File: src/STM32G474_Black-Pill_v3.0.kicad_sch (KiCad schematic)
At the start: 45 parts, among them J101 USB_C_Receptacle_USB2.0, J102 Conn_01x20, J103 Conn_01x20, J104 Conn_01x04, SW101 SW_Push, SW102 SW_Push, SW103 SW_Push, U101 W25Q32JVSS, U102 STM32G474RETx, U103 AP7343xx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

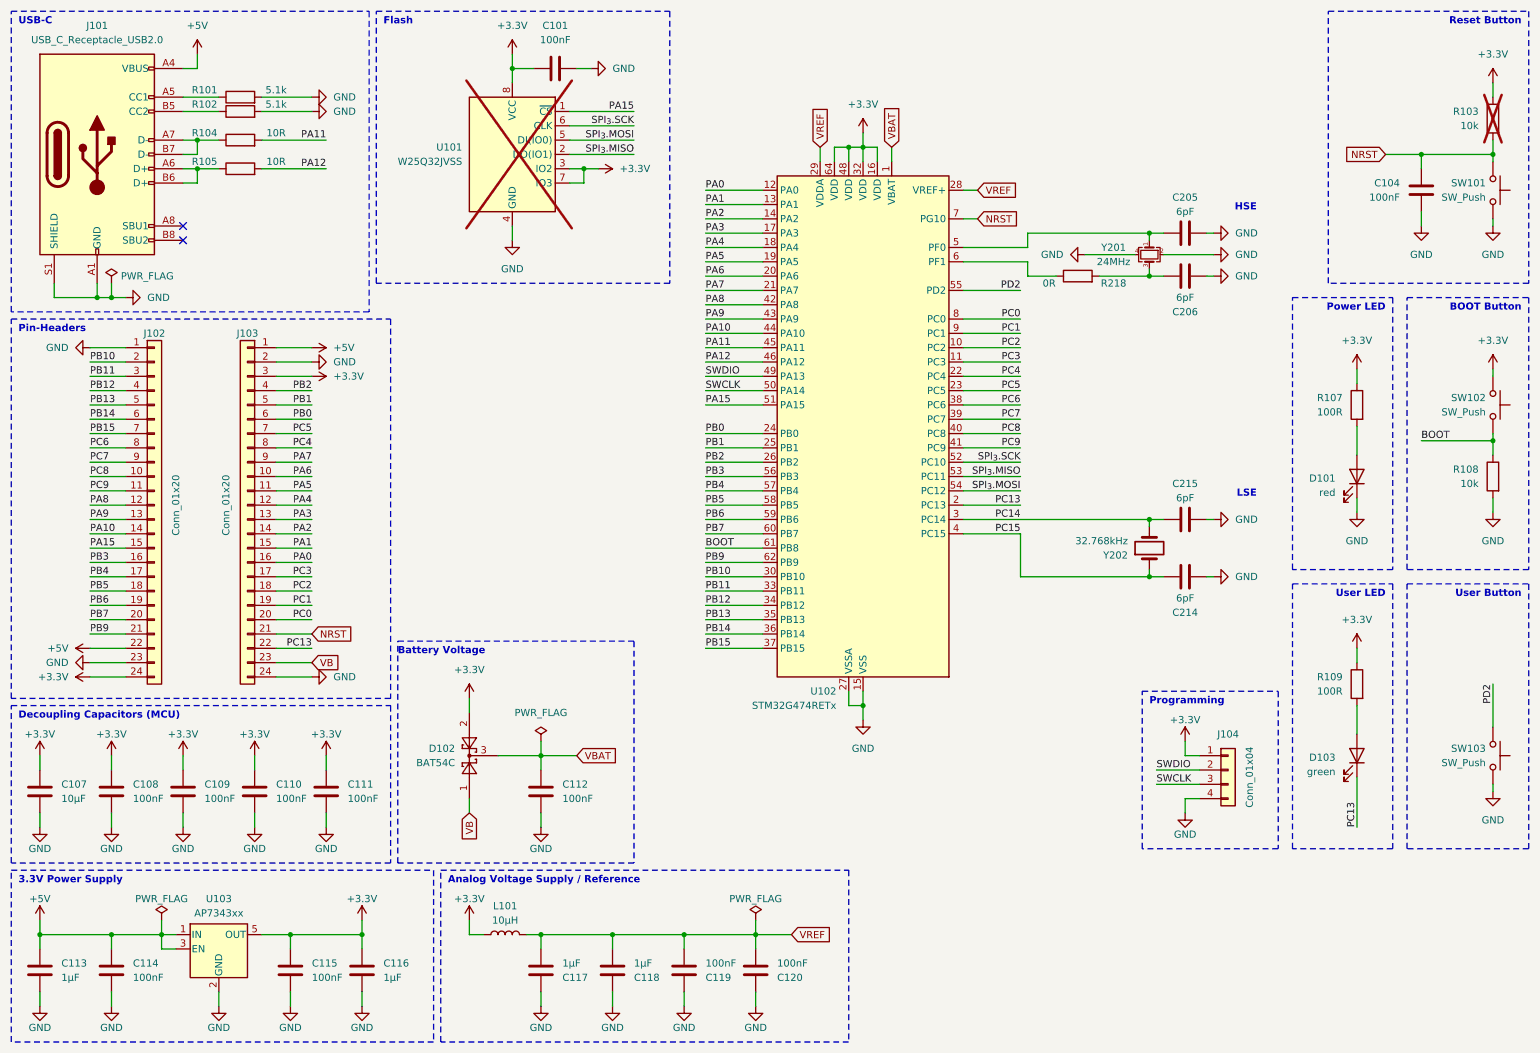
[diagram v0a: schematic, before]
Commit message: Mod: STM32G474_Black-Pill_v3.0.kicad_pcb, changed footprint of STM32G474 and the whole PCB has to be adjusted.
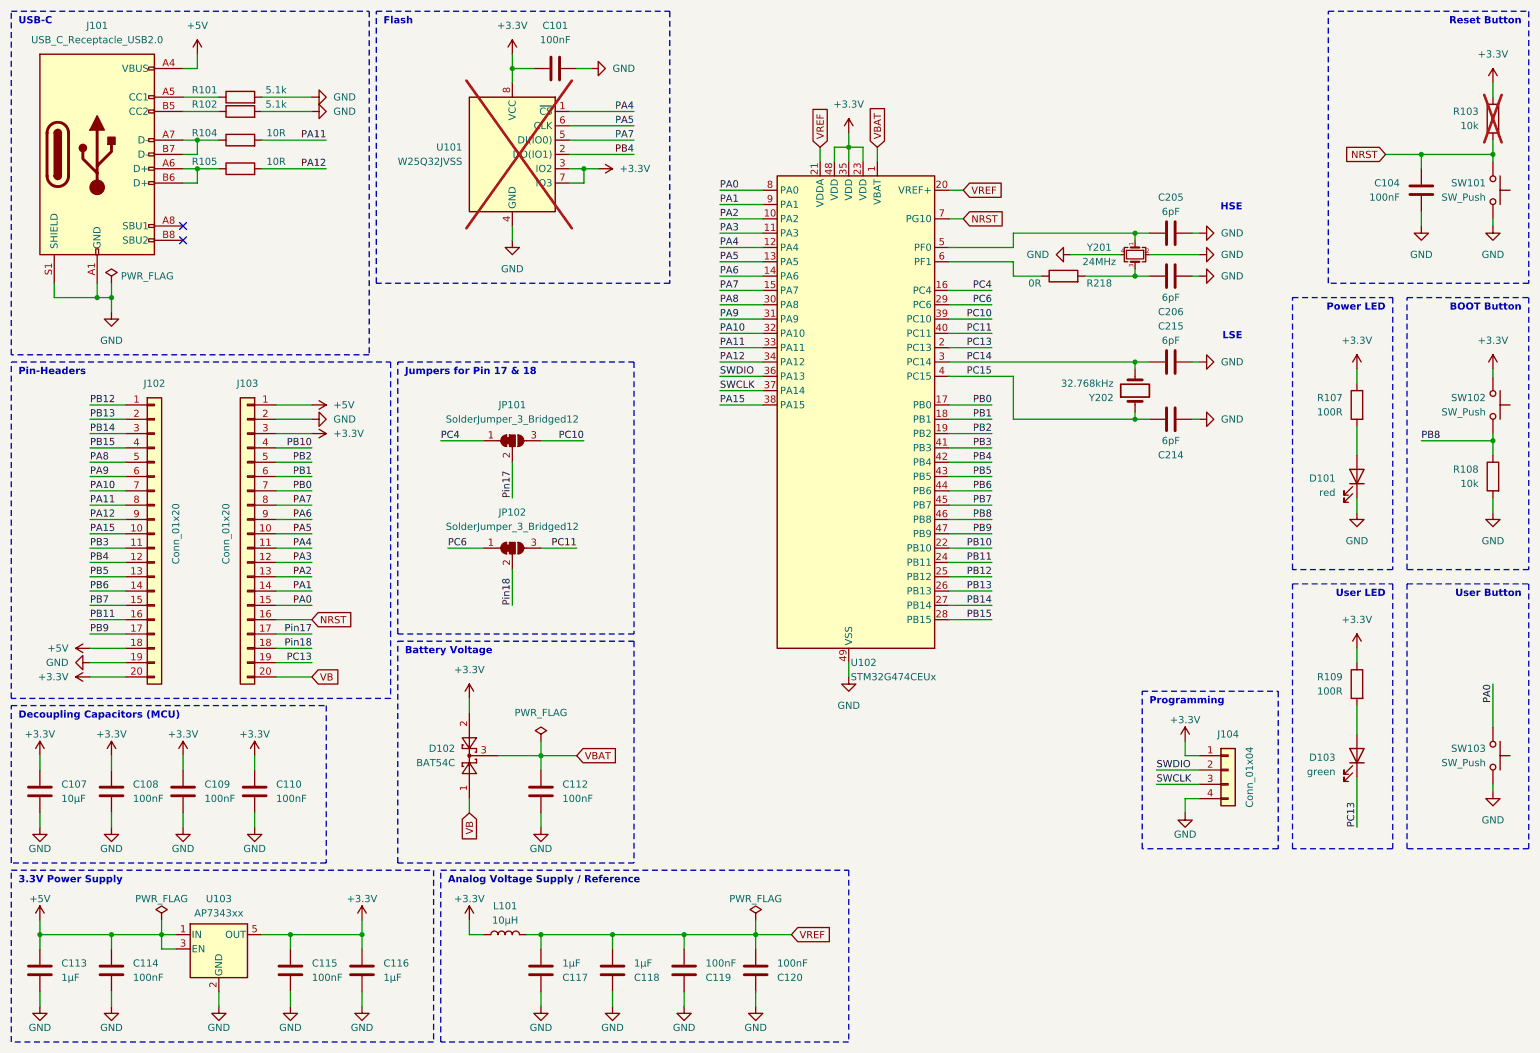
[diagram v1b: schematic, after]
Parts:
- removed C111: 100nF, Capacitor_SMD:C_0402_1005Metric, symbol Device:C
- removed U102: STM32G474RETx, Package_QFP:LQFP-64_10x10mm_P0.5mm, symbol MCU_ST_STM32G4:STM32G474RETx
- added JP101, JP102: SolderJumper_3_Bridged12, Jumper:SolderJumper-3_P1.3mm_Bridged12_RoundedPad1.0x1.5mm_NumberLabels, symbol Jumper:SolderJumper_3_Bridged12
- added U102: STM32G474CEUx, Package_DFN_QFN:QFN-48-1EP_7x7mm_P0.5mm_EP5.6x5.6mm, symbol MCU_ST_STM32G4:STM32G474CEUx
- J102, J103: footprint Connector_PinHeader_2.54mm:PinHeader_1x24_P2.54mm_Vertical -> Connector_PinHeader_2.54mm:PinHeader_1x20_P2.54mm_Vertical; symbol Connector_Generic:Conn_01x24 -> Connector_Generic:Conn_01x20
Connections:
- net PC0 is gone; now on net VB: J103.20 (Pin_20)
- net PC1 is gone; now on net PC13: J103.19 (Pin_19)
- net PC5 is gone; now on net PB0: J103.7 (Pin_7)
- net PC7 is gone; now on net PA12: J102.9 (Pin_9)
- net PC8 is gone; now on net PA15: J102.10 (Pin_10)
- net PC9 is gone; now on net PB3: J102.11 (Pin_11)
- net PD2 is gone; now on net PA0: SW103.2
- net SPI_{3}.MISO is gone; now on net PB4: U101.2 (DO(IO1))
- net SPI_{3}.MOSI is gone; now on net PA7: U101.5 (DI(IO0))
- net SPI_{3}.SCK is gone; now on net PA5: U101.6 (CLK)
- net +3.3V: now also J102.20 (Pin_20), U102.23 (VDD), U102.35 (VDD), U102.48 (VDD); no longer J102.24 (Pin_24)
- net +5V: now also J102.18 (Pin_18); no longer J102.22 (Pin_22)
- net GND: now also J102.19 (Pin_19), U102.49 (VSS); no longer J102.1 (Pin_1), J102.23 (Pin_23), J103.24 (Pin_24)
- net NRST: now also J103.16 (Pin_16), U102.7 (PG10); no longer J103.21 (Pin_21)
- net PA0: now also J103.15 (Pin_15), U102.8 (PA0); no longer J103.16 (Pin_16)
- net PA1: now also J103.14 (Pin_14), U102.9 (PA1); no longer J103.15 (Pin_15)
- net PA10: now also J102.7 (Pin_7), U102.32 (PA10); no longer J102.14 (Pin_14)
- net PA11: now also J102.8 (Pin_8), U102.33 (PA11)
- net PA12: now also U102.34 (PA12)
- net PA15: now also U102.38 (PA15); no longer J102.15 (Pin_15), U101.1 (~{CS})
- net PA2: now also J103.13 (Pin_13), U102.10 (PA2); no longer J103.14 (Pin_14)
- net PA3: now also J103.12 (Pin_12), U102.11 (PA3); no longer J103.13 (Pin_13)
- net PA4: now also J103.11 (Pin_11), U101.1 (~{CS}), U102.12 (PA4); no longer J103.12 (Pin_12)
- net PA5: now also J103.10 (Pin_10), U102.13 (PA5); no longer J103.11 (Pin_11)
- net PA6: now also J103.9 (Pin_9), U102.14 (PA6); no longer J103.10 (Pin_10)
- net PA7: now also J103.8 (Pin_8), U102.15 (PA7); no longer J103.9 (Pin_9)
- net PA8: now also J102.5 (Pin_5), U102.30 (PA8); no longer J102.12 (Pin_12)
- net PA9: now also J102.6 (Pin_6), U102.31 (PA9); no longer J102.13 (Pin_13)
- net PB0: now also U102.17 (PB0); no longer J103.6 (Pin_6)
- net PB1: now also J103.6 (Pin_6), U102.18 (PB1); no longer J103.5 (Pin_5)
- net PB10: now also J103.4 (Pin_4), U102.22 (PB10); no longer J102.2 (Pin_2)
- net PB11: now also J102.16 (Pin_16), U102.24 (PB11); no longer J102.3 (Pin_3)
- net PB12: now also J102.1 (Pin_1), U102.25 (PB12); no longer J102.4 (Pin_4)
- net PB13: now also J102.2 (Pin_2), U102.26 (PB13); no longer J102.5 (Pin_5)
- net PB14: now also J102.3 (Pin_3), U102.27 (PB14); no longer J102.6 (Pin_6)
- net PB15: now also J102.4 (Pin_4), U102.28 (PB15); no longer J102.7 (Pin_7)
- net PB2: now also J103.5 (Pin_5), U102.19 (PB2); no longer J103.4 (Pin_4)
- net PB3: now also U102.41 (PB3); no longer J102.16 (Pin_16)
- net PB4: now also J102.12 (Pin_12), U102.42 (PB4); no longer J102.17 (Pin_17)
- net PB5: now also J102.13 (Pin_13), U102.43 (PB5); no longer J102.18 (Pin_18)
- net PB6: now also J102.14 (Pin_14), U102.44 (PB6); no longer J102.19 (Pin_19)
- net PB7: now also J102.15 (Pin_15), U102.45 (PB7); no longer J102.20 (Pin_20)
- net PB9: now also J102.17 (Pin_17), U102.47 (PB9); no longer J102.21 (Pin_21)
- net PC13: now also U102.2 (PC13); no longer J103.22 (Pin_22)
- net PC14: now also U102.3 (PC14)
- net PC15: now also U102.4 (PC15)
- net PC4: now also JP101.1 (A), U102.16 (PC4); no longer J103.8 (Pin_8)
- net PC6: now also JP102.1 (A), U102.29 (PC6); no longer J102.8 (Pin_8)
- net SWCLK: now also U102.37 (PA14)
- net SWDIO: now also U102.36 (PA13)
- net VB: no longer J103.23 (Pin_23)
- net VBAT: now also U102.1 (VBAT)
- net VREF: now also U102.20 (VREF+), U102.21 (VDDA)
- net at C205.2, Y201.1: now also U102.5 (PF0)
- net at R218.1: now also U102.6 (PF1)
- net BOOT renamed PB8
- net PB8: now also U102.46 (PB8)
- net PC2 renamed Pin18
- net Pin18: now also JP102.2 (C)
- net PC3 renamed Pin17
- net Pin17: now also JP101.2 (C)
- new net PC10: JP101.3 (B), U102.39 (PC10)
- new net PC11: JP102.3 (B), U102.40 (PC11)
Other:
- note added: "Jumpers for Pin 17 & 18"
- moved on the sheet: C205, C206, C214, C215, R218, Y201, Y202

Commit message: Mod: PCB and Schematic, re-exported all files.
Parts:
- added JP103: SolderJumper_2_Bridged, Jumper:SolderJumper-2_P1.3mm_Bridged_RoundedPad1.0x1.5mm, symbol Jumper:SolderJumper_2_Bridged
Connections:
- net +3.3V: now also JP103.2 (B); no longer C107.1, C108.1, C109.1, C110.1, U102.23 (VDD), U102.35 (VDD), U102.48 (VDD)
- new net +3.3V_{MCU}: C107.1, C108.1, C109.1, C110.1, JP103.1 (A), U102.23 (VDD), U102.35 (VDD), U102.48 (VDD)
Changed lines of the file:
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@@
   (junction (at 213.36 76.2) (diameter 0) (color 0 0 0 0)
   )
+  (junction (at 44.45 146.05) (diameter 0) (color 0 0 0 0)
+  )
   (junction (at 31.75 177.8) (diameter 0) (color 0 0 0 0)
   )
@@
   (junction (at 102.87 24.13) (diameter 0) (color 0 0 0 0)
   )
+  (junction (at 57.15 146.05) (diameter 0) (color 0 0 0 0)
+  )
   (junction (at 115.57 41.91) (diameter 0) (color 0 0 0 0)
   )
+  (junction (at 31.75 146.05) (diameter 0) (color 0 0 0 0)
+  )
   (junction (at 276.86 90.17) (diameter 0) (color 0 0 0 0)
   )
@@
     (stroke (width 0) (type default))
   )
+  (wire (pts (xy 19.05 146.05) (xy 31.75 146.05))
+    (stroke (width 0) (type default))
+  )
   (wire (pts (xy 46.99 24.13) (xy 46.99 21.59))
     (stroke (width 0) (type default))
@@
     (stroke (width 0) (type default))
   )
-  (wire (pts (xy 162.56 35.56) (xy 162.56 38.1))
+  (wire (pts (xy 162.56 27.94) (xy 162.56 38.1))
+    (stroke (width 0) (type default))
+  )
+  (wire (pts (xy 31.75 146.05) (xy 44.45 146.05))
     (stroke (width 0) (type default))
   )
@@
     (stroke (width 0) (type default))
   )
+  (wire (pts (xy 63.5 146.05) (xy 57.15 146.05))
+    (stroke (width 0) (type default))
+  )
   (wire (pts (xy 222.25 146.05) (xy 224.79 146.05))
     (stroke (width 0) (type default))
@@
     (stroke (width 0) (type default))
   )
+  (wire (pts (xy 76.2 146.05) (xy 71.12 146.05))
+    (stroke (width 0) (type default))
+  )
   (wire (pts (xy 139.7 63.5) (xy 147.32 63.5))
     (stroke (width 0) (type default))
@@
     (stroke (width 0) (type default))
   )
+  (wire (pts (xy 76.2 143.51) (xy 76.2 146.05))
+    (stroke (width 0) (type default))
+  )
   (wire (pts (xy 196.85 60.96) (xy 191.77 60.96))
     (stroke (width 0) (type default))
@@
     (stroke (width 0) (type default))
   )
+  (wire (pts (xy 44.45 146.05) (xy 57.15 146.05))
+    (stroke (width 0) (type default))
+  )
   (wire (pts (xy 160.02 40.64) (xy 160.02 38.1))
     (stroke (width 0) (type default))
@@
     (fill (type none))
   )
-  (rectangle (start 13.97 137.16) (end 69.85 165.1)
+  (rectangle (start 13.97 137.16) (end 81.28 165.1)
     (stroke (width 0) (type dash))
     (fill (type none))
@@
     (effects (font (size 1.27 1.27)) (justify right bottom))
   )
+  (label "+3.3V_{MCU}" (at 162.56 27.94 270) (fields_autoplaced)
+    (effects (font (size 1.27 1.27)) (justify right bottom))
+  )
+  (label "+3.3V_{MCU}" (at 19.05 146.05 0) (fields_autoplaced)
+    (effects (font (size 1.27 1.27)) (justify left bottom))
+  )
   (label "PA2" (at 67.31 114.3 180) (fields_autoplaced)
     (effects (font (size 1.27 1.27)) (justify right bottom))
@@
     )
   )
-  (symbol (lib_id "power:+3.3V") (at 44.45 146.05 0) (unit 1)
-    (in_bom yes) (on_board yes) (dnp no)
-    (property "Reference" "#PWR0135" (at 44.45 149.86 0)
-      (effects (font (size 1.27 1.27)) hide)
-    )
-    (property "Value" "+3.3V" (at 44.45 142.24 0)
-      (effects (font (size 1.27 1.27)))
-    )
-    (property "Footprint" "" (at 44.45 146.05 0)
-      (effects (font (size 1.27 1.27)) hide)
-    )
-    (property "Datasheet" "" (at 44.45 146.05 0)
-      (effects (font (size 1.27 1.27)) hide)
-    )
-    (pin "1")
-    (instances
-      (project "STM32G474_Black-Pill_v3.0"
-        (path "/bfaac094-0365-40a4-8b7a-d4d62ace544e"
-          (reference "#PWR0135") (unit 1)
-        )
-      )
-    )
-  )
   (symbol (lib_id "Device:C") (at 133.35 184.15 0) (mirror x) (unit 1)
     (in_bom yes) (on_board yes) (dnp no) (fields_autoplaced)
@@
     )
   )
-  (symbol (lib_id "power:+3.3V") (at 162.56 35.56 0) (mirror y) (unit 1)
-    (in_bom yes) (on_board yes) (dnp no) (fields_autoplaced)
-    (property "Reference" "#PWR0103" (at 162.56 39.37 0)
-      (effects (font (size 1.27 1.27)) hide)
-    )
-    (property "Value" "+3.3V" (at 162.56 30.48 0)
-      (effects (font (size 1.27 1.27)))
-    )
-    (property "Footprint" "" (at 162.56 35.56 0)
-      (effects (font (size 1.27 1.27)) hide)
-    )
-    (property "Datasheet" "" (at 162.56 35.56 0)
-      (effects (font (size 1.27 1.27)) hide)
-    )
-    (pin "1")
-    (instances
-      (project "STM32G474_Black-Pill_v3.0"
-        (path "/bfaac094-0365-40a4-8b7a-d4d62ace544e"
-          (reference "#PWR0103") (unit 1)
-        )
-      )
-    )
-  )
   (symbol (lib_id "Connector:USB_C_Receptacle_USB2.0") (at 29.21 39.37 0) (unit 1)
     (in_bom yes) (on_board yes) (dnp no) (fields_autoplaced)
@@
     )
   )
-  (symbol (lib_id "power:+3.3V") (at 31.75 146.05 0) (unit 1)
+  (symbol (lib_id "power:+3.3V") (at 76.2 143.51 0) (unit 1)
     (in_bom yes) (on_board yes) (dnp no)
-    (property "Reference" "#PWR0134" (at 31.75 149.86 0)
+    (property "Reference" "#PWR0134" (at 76.2 147.32 0)
       (effects (font (size 1.27 1.27)) hide)
     )
-    (property "Value" "+3.3V" (at 31.75 142.24 0)
+    (property "Value" "+3.3V" (at 76.2 139.7 0)
       (effects (font (size 1.27 1.27)))
     )
-    (property "Footprint" "" (at 31.75 146.05 0)
+    (property "Footprint" "" (at 76.2 143.51 0)
       (effects (font (size 1.27 1.27)) hide)
     )
-    (property "Datasheet" "" (at 31.75 146.05 0)
+    (property "Datasheet" "" (at 76.2 143.51 0)
       (effects (font (size 1.27 1.27)) hide)
     )
@@
     )
   )
-  (symbol (lib_id "power:+3.3V") (at 57.15 146.05 0) (unit 1)
-    (in_bom yes) (on_board yes) (dnp no)
-    (property "Reference" "#PWR0136" (at 57.15 149.86 0)
-      (effects (font (size 1.27 1.27)) hide)
-    )
-    (property "Value" "+3.3V" (at 57.15 142.24 0)
-      (effects (font (size 1.27 1.27)))
-    )
-    (property "Footprint" "" (at 57.15 146.05 0)
-      (effects (font (size 1.27 1.27)) hide)
-    )
-    (property "Datasheet" "" (at 57.15 146.05 0)
-      (effects (font (size 1.27 1.27)) hide)
-    )
-    (pin "1")
-    (instances
-      (project "STM32G474_Black-Pill_v3.0"
-        (path "/bfaac094-0365-40a4-8b7a-d4d62ace544e"
-          (reference "#PWR0136") (unit 1)
-        )
-      )
-    )
-  )
   (symbol (lib_id "power:GND") (at 276.86 52.07 0) (mirror y) (unit 1)
     (in_bom yes) (on_board yes) (dnp no) (fields_autoplaced)
@@
     )
   )
-  (symbol (lib_id "power:+3.3V") (at 19.05 146.05 0) (unit 1)
+  (symbol (lib_id "Jumper:SolderJumper_2_Bridged") (at 67.31 146.05 0) (unit 1)
     (in_bom yes) (on_board yes) (dnp no)
-    (property "Reference" "#PWR0133" (at 19.05 149.86 0)
-      (effects (font (size 1.27 1.27)) hide)
-    )
-    (property "Value" "+3.3V" (at 19.05 142.24 0)
+    (property "Reference" "JP103" (at 67.31 139.7 0)
       (effects (font (size 1.27 1.27)))
     )
-    (property "Footprint" "" (at 19.05 146.05 0)
+    (property "Value" "SolderJumper_2_Bridged" (at 71.12 142.24 0)
+      (effects (font (size 1.27 1.27)) (justify right))
+    )
+    (property "Footprint" "Jumper:SolderJumper-2_P1.3mm_Bridged_RoundedPad1.0x1.5mm" (at 67.31 146.05 0)
       (effects (font (size 1.27 1.27)) hide)
     )
-    (property "Datasheet" "" (at 19.05 146.05 0)
+    (property "Datasheet" "~" (at 67.31 146.05 0)
       (effects (font (size 1.27 1.27)) hide)
     )
     (pin "1")
+    (pin "2")
     (instances
       (project "STM32G474_Black-Pill_v3.0"
         (path "/bfaac094-0365-40a4-8b7a-d4d62ace544e"
-          (reference "#PWR0133") (unit 1)
+          (reference "JP103") (unit 1)
         )
       )
